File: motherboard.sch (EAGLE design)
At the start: 185 parts, among them IC1 LM2576, IC10 TUSB2046B, IC12 LM50, IC13 LM50, IC2 74LS595D, IC3 74LS595D, IC4 IC_FT230X-SSOP-16, IC5 VN5772AK, IC6 VN5772AK, IC7 VN5772AK, IC8 VN5772AK, IC9 VN5772AK, SW1 FSMSM, U2 NCP4625, U3 ATMEGA168, Y1 16Mhz, Y2 6MHz

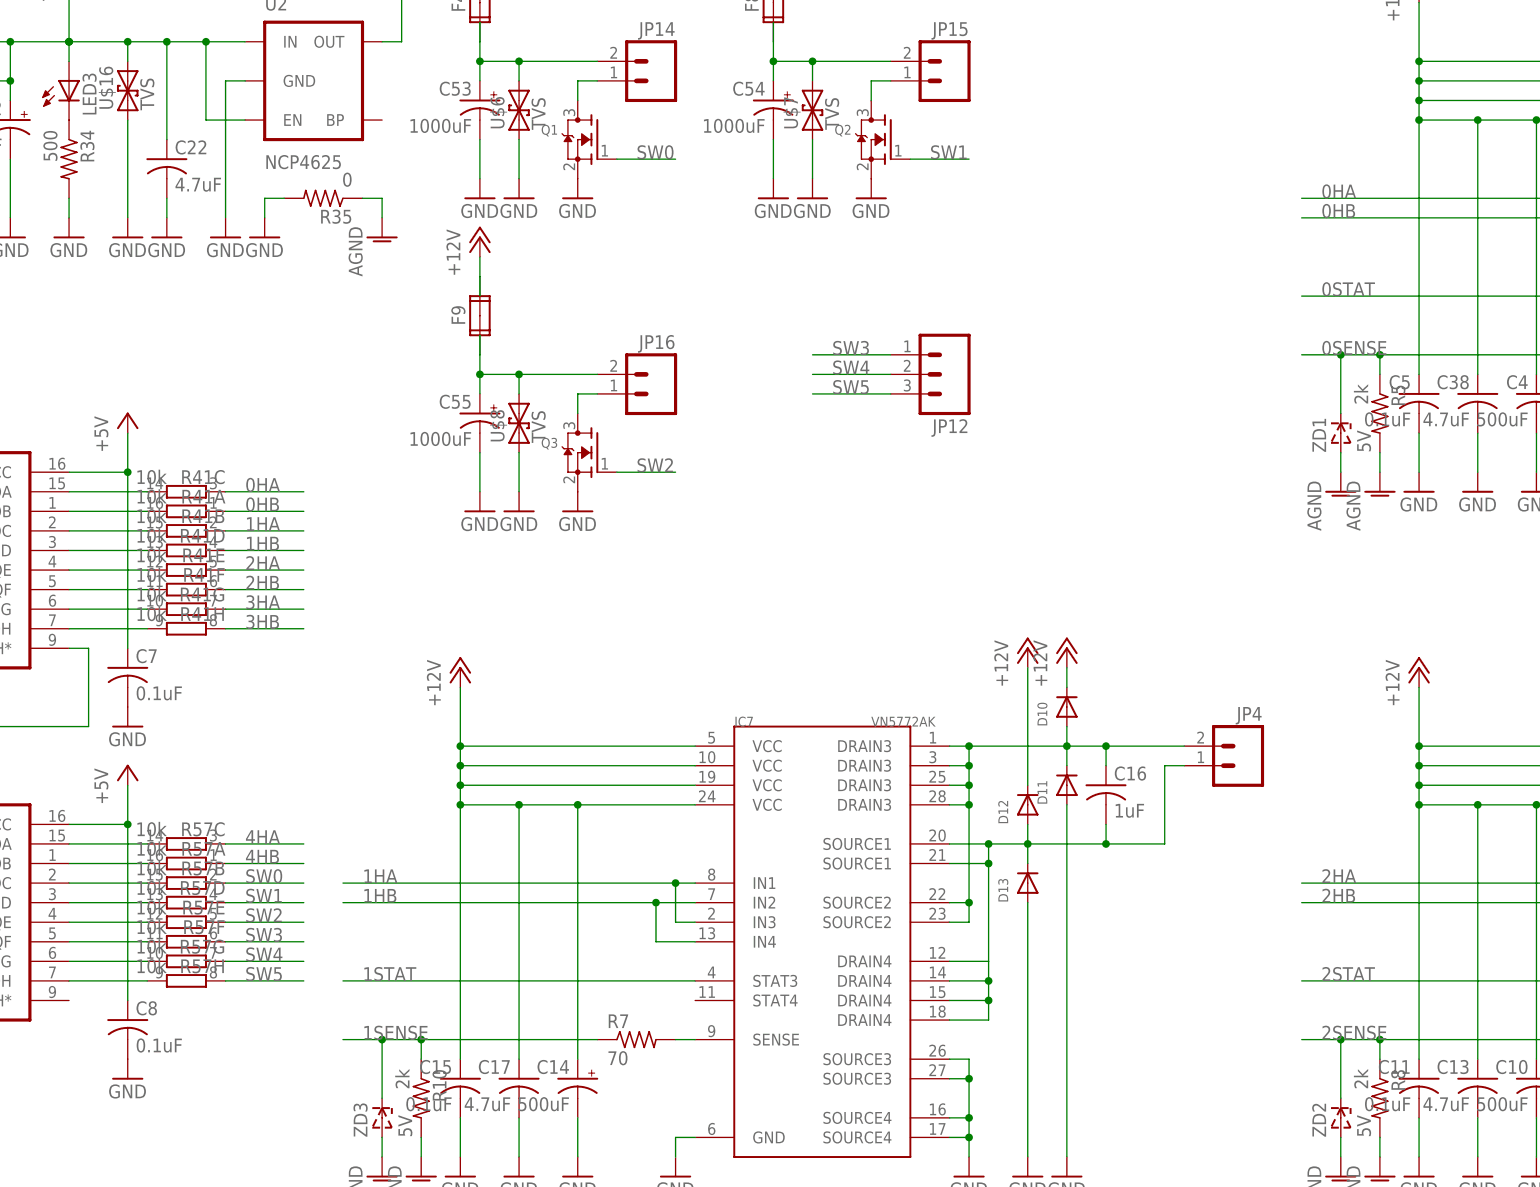
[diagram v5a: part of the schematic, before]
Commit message: layed out control lines to hbridges, fets
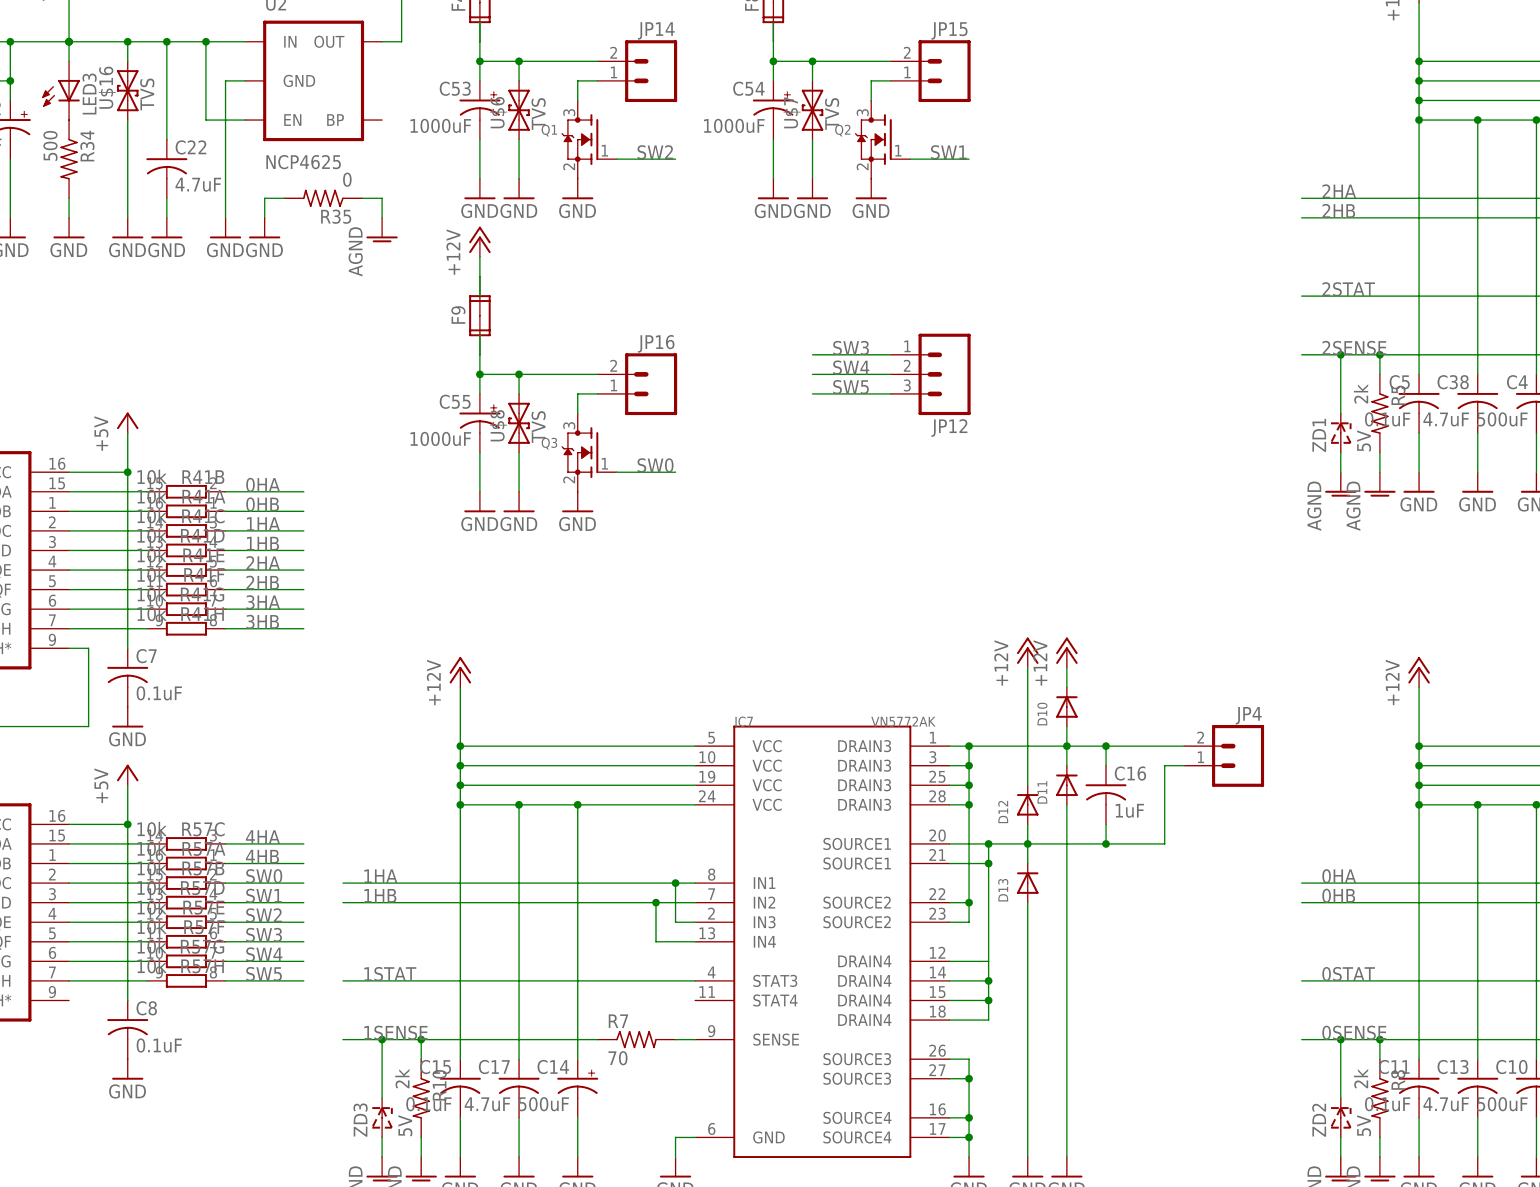
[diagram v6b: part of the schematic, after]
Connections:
- net 0HA: now also IC6.IN1, IC6.IN3, R41B.1; no longer IC5.IN1, IC5.IN3, R41C.1
- net 0HB: now also IC6.IN2, IC6.IN4; no longer IC5.IN2, IC5.IN4
- net 0SENSE: now also R8.1, R9.1, ZD2.C; no longer R5.1, R6.1, ZD1.C
- net 0STAT: now also IC6.STAT3; no longer IC5.STAT3
- net 1HA: now also R41C.1; no longer R41B.1
- net 2HA: now also IC5.IN1, IC5.IN3; no longer IC6.IN1, IC6.IN3
- net 2HB: now also IC5.IN2, IC5.IN4; no longer IC6.IN2, IC6.IN4
- net 2SENSE: now also R5.1, R6.1, ZD1.C; no longer R8.1, R9.1, ZD2.C
- net 2STAT: now also IC5.STAT3; no longer IC6.STAT3
- net N$69: now also R41C.2; no longer R41B.2
- net N$71: now also R41B.2; no longer R41C.2
- net SW0: now also Q3.G; no longer Q1.G
- net SW2: now also Q1.G; no longer Q3.G
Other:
- moved on the sheet: R41B, R41C

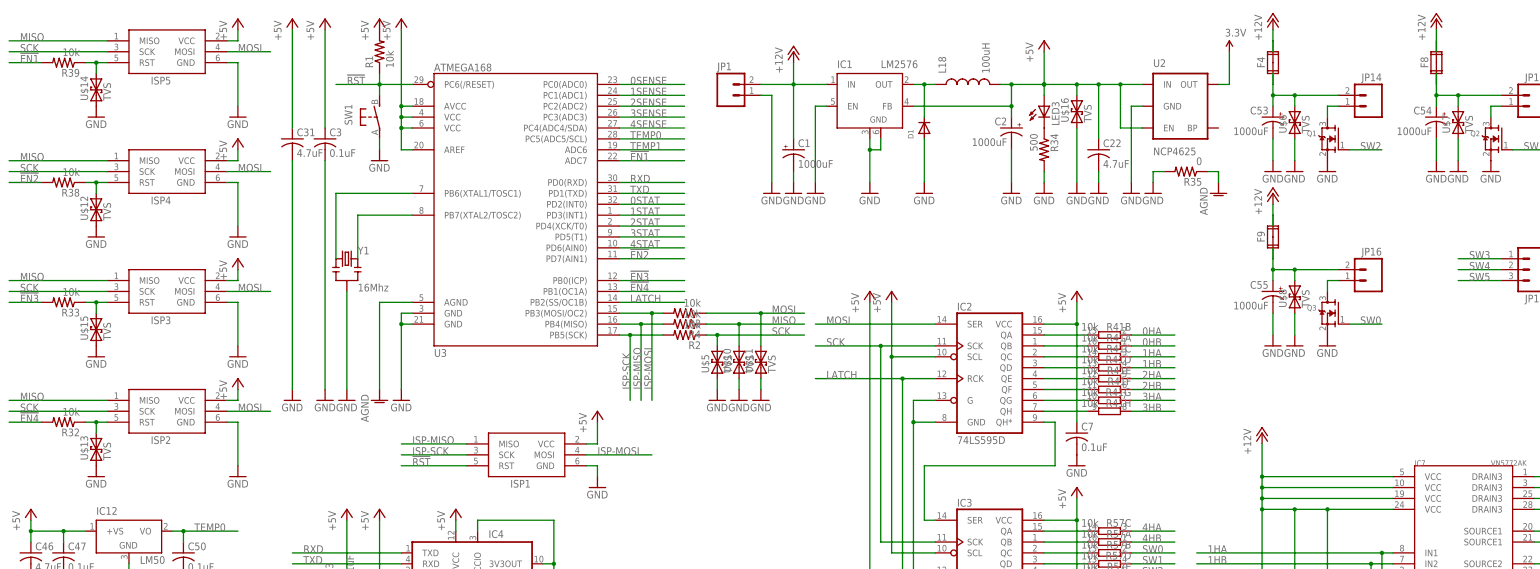
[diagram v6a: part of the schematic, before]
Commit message: laying out mcu
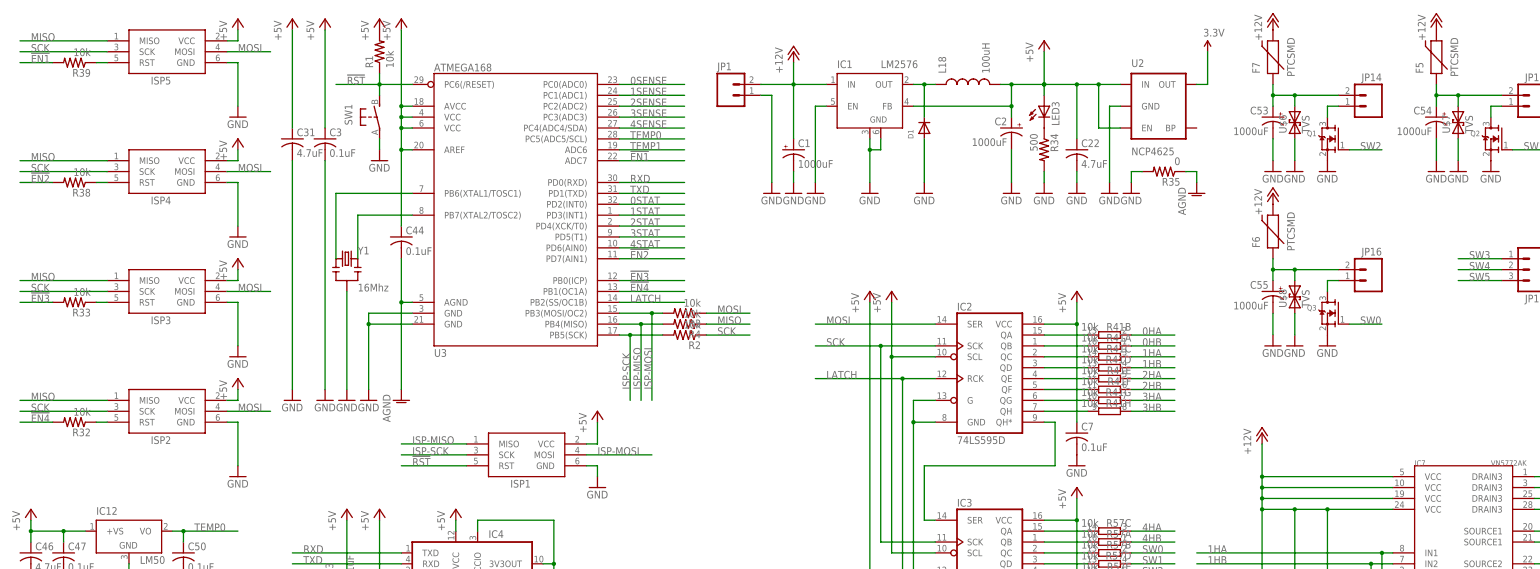
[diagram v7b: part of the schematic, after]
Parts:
- removed F4, F8, F9: 3557-2, rov_club:3557-2
- removed U$10, U$11, U$12, U$13, U$14, U$15, U$16, U$5: TVS, sparkfun:TVS
- added C44: 0.1uF, adafruit:C-USC1206
- added F5, F6, F7: PTCSMD, sparkfun:PTCSMD
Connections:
- net +12V: now also F5.2, F6.2, F7.2; no longer F4.2A, F4.2B, F8.2A, F8.2B, F9.2A, F9.2B
- net +5V: now also C44.1; no longer U$16.2
- net AGND: now also C44.2
- net GND: no longer U$10.1, U$11.1, U$12.1, U$13.1, U$14.1, U$15.1, U$16.1, U$5.1
- net MISO: no longer U$10.2
- net MOSI: no longer U$11.2
- net N$50: now also F6.1; no longer F9.1A, F9.1B
- net N$51: no longer U$13.2
- net N$52: no longer U$15.2
- net N$53: no longer U$12.2
- net N$54: now also F5.1; no longer F8.1A, F8.1B
- net N$55: now also F7.1; no longer F4.1A, F4.1B
- net N$58: no longer U$14.2
- net SCK: no longer U$5.2
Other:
- moved on the sheet: C22, R32, R33, R35, R38, R39, U2

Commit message: ...
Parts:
- added JP10, JP7, JP9: (no value), sparkfun:M02PTH
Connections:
- net +12V: now also JP10.2, JP7.2, JP9.2
- net N$50: now also JP10.1
- net N$54: now also JP9.1
- net N$55: now also JP7.1
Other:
- moved on the sheet: C53, C54, C55, F5, F6, F7, JP12, JP14, JP15, JP16, Q1, Q2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
